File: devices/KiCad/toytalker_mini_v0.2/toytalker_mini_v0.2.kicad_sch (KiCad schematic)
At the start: 29 parts, among them J1 TYPE-C-31-M-12, J2 SM02B-SRSS-TB(LF)(SN), U1 BQ25185DLHR, U2 AP2112K-3.3TRG1, U3 ESP32-S3-MINI-1-N4R2, U4 MAX98357AEWL_T

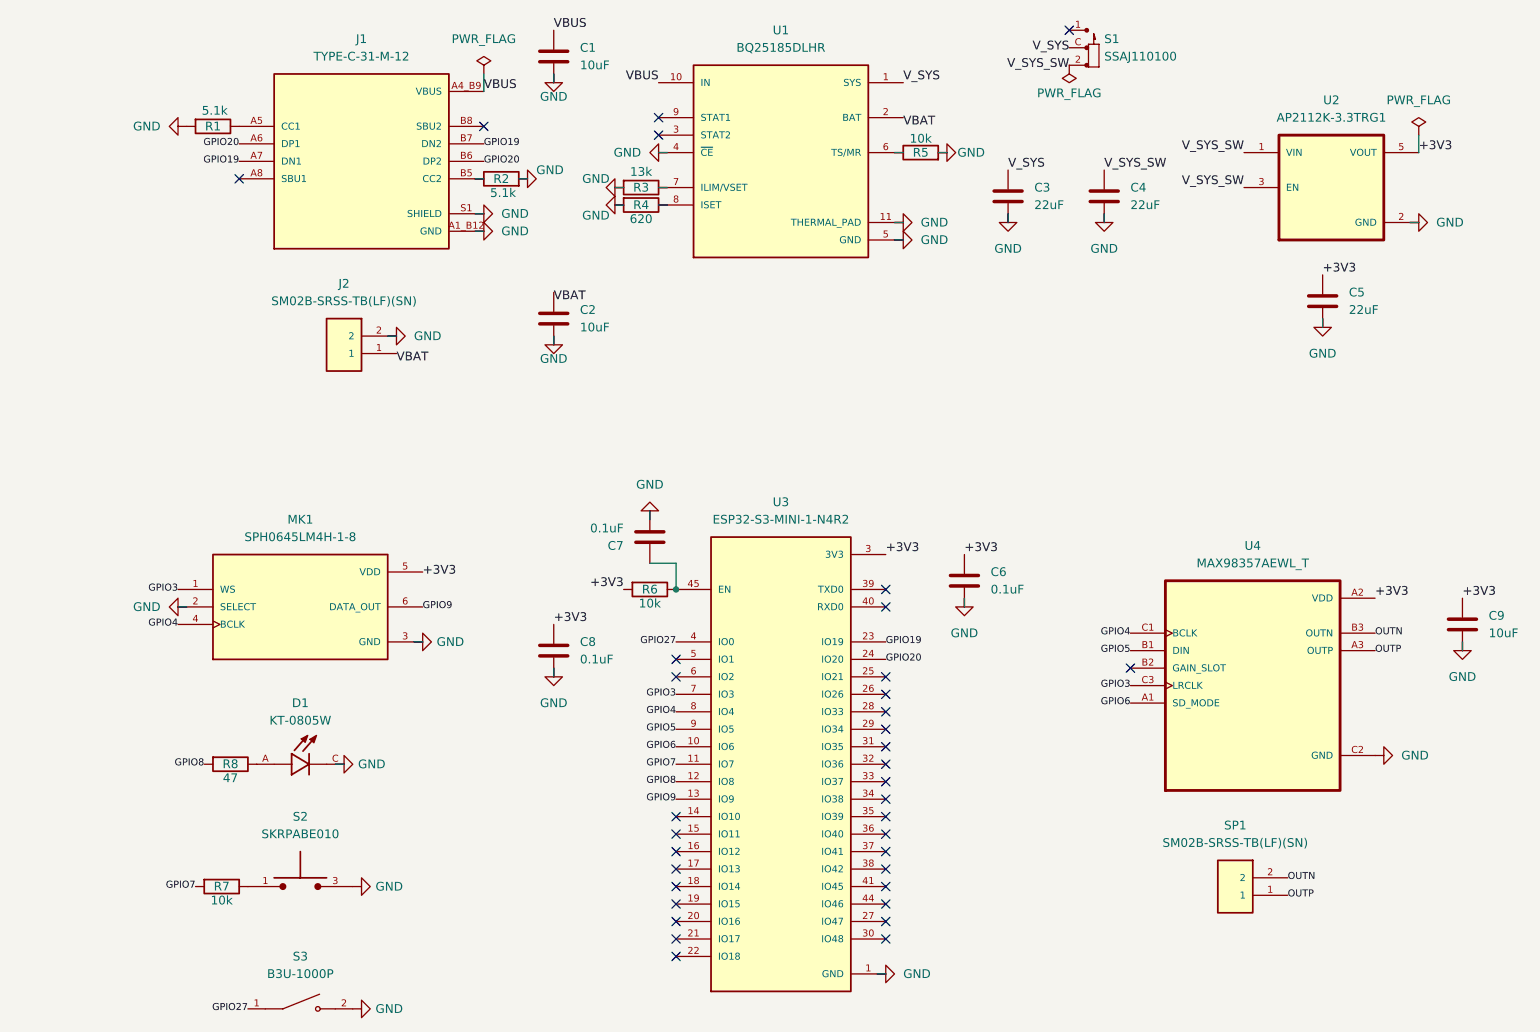
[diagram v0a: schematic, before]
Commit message: Complete v0.2 schematic: ERC clean, new parts, temp sensing, EN-mode power
- New connectors: J2=JST ZH (S2B-ZR-SM4A-TF), SP1=HC-1.25-2PWT (MX1.25),
  S1=MSK12C02G15-B slide switch in EN-mode (signal-only via PWR_EN + R9 100k)
- Charge temp protection: TH1 (NCP15XH103F03RC) on BQ25185 TS/MR
- Board temp readout: TH2 + R14 divider on GPIO2 (ADC1_CH1)
- Battery voltage divider on GPIO1, STAT1/2 to GPIO13/14 with 100k pullups
- LED R8 47R -> 470R, amp VDD direct to V_SYS, I2S pins separated
- Fix BQ25185 SYS pin type to power_out; footprint links now use
  project 'footprints' lib; register 3 missing symbol libs project-locally
- ERC: 0 errors, 0 warnings; all nets verified against PINMAP.md via netlist

Co-Authored-By: Claude Fable 5 <noreply@anthropic.com>
Claude-Session: https://claude.ai/code/session_017Se8MNjUgWCs8o61hRDxnG
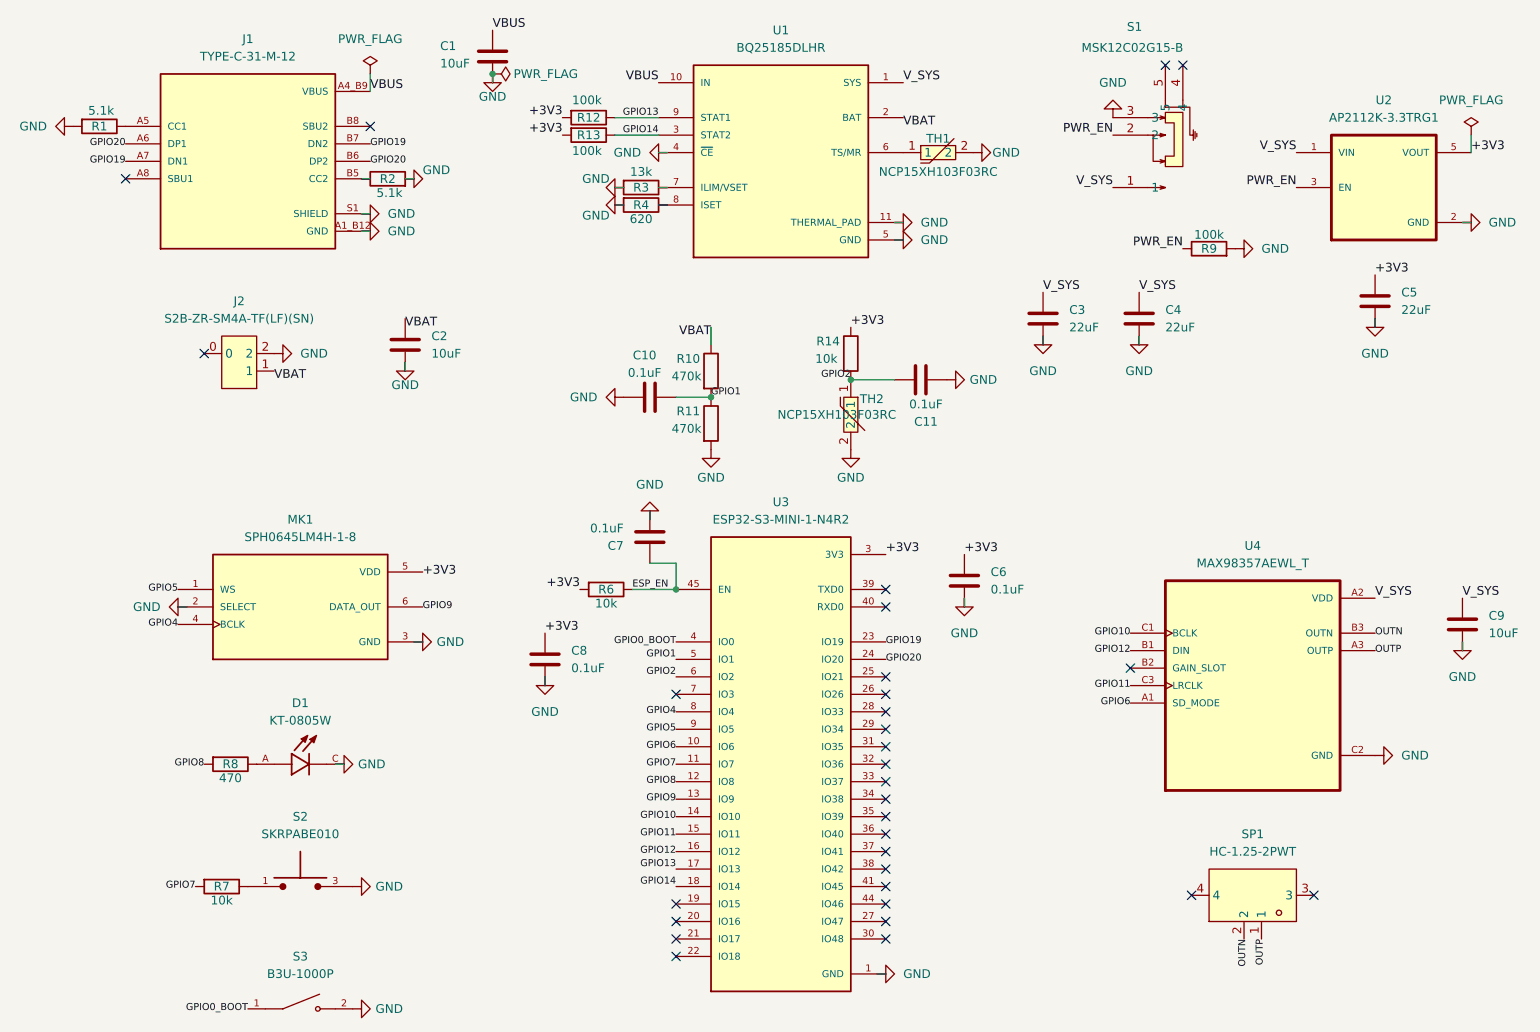
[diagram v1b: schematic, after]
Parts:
- removed J2, SP1: SM02B-SRSS-TB(LF)(SN), footprints:SM02B-SRSS-TB_LF__SN_, symbol SM02B-SRSS-TB_LF__SN_:SM02B-SRSS-TB_LF__SN_
- removed R5: 10k, Resistor_SMD:R_0402_1005Metric, symbol Device:R
- removed S1: SSAJ110100, footprints:SW_SSAJ110100, symbol SSAJ110100:SSAJ110100
- added C10, C11: 0.1uF, Capacitor_SMD:C_0603_1608Metric, symbol Device:C
- added J2: S2B-ZR-SM4A-TF(LF)(SN), toytalker_v02_parts:CONN-SMD_S2B-ZR-SM4A, symbol toytalker_v02_parts:S2B-ZR-SM4A-TF(LF)(SN)
- added R10, R11: 470k, Resistor_SMD:R_0402_1005Metric, symbol Device:R
- added R12, R13, R9: 100k, Resistor_SMD:R_0402_1005Metric, symbol Device:R
- added R14: 10k, Resistor_SMD:R_0402_1005Metric, symbol Device:R
- added S1: MSK12C02G15-B, toytalker_v02_parts:SW-SMD_MSK12C02G15-B, symbol toytalker_v02_parts:MSK12C02G15-B
- added SP1: HC-1.25-2PWT, toytalker_v02_parts:CONN-SMD_2P-P1.25-HC-1.25-2PWT, symbol toytalker_v02_parts:HC-1.25-2PWT
- added TH1, TH2: NCP15XH103F03RC, toytalker_v02_parts:R0402, symbol toytalker_v02_parts:NCP15XH103F03RC
- R8: value 47 -> 470
- S3: footprint Button_Switch_SMD:SW_SPST_B3U-1000P -> footprints:SW_B3U-1000P
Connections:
- net +3V3: now also R12.2, R13.2, R14.1; no longer C9.1, U4.A2 (VDD)
- net GND: now also C10.2, C11.2, J2.2, R11.2, R9.2, S1.3, TH1.2, TH2.2
- net GPIO4: no longer U4.C1 (BCLK)
- net GPIO5: now also MK1.1 (WS); no longer U4.B1 (DIN)
- net OUTN: now also SP1.2
- net OUTP: now also SP1.1
- net VBAT: now also J2.1, R10.1
- net V_SYS: now also C4.1, C9.1, U2.1 (VIN), U4.A2 (VDD), S1.1
- net at U1.6 (TS/MR): now also TH1.1
- net ESP_EN: now reaches C7.1, R6.1, U3.45 (EN)
- net GPIO10: now reaches U3.14 (IO10)
- net GPIO10: now also U4.C1 (BCLK)
- net GPIO11: now reaches U3.15 (IO11)
- net GPIO11: now also U4.C3 (LRCLK)
- net GPIO12: now reaches U3.16 (IO12)
- net GPIO12: now also U4.B1 (DIN)
- net GPIO13: now reaches U3.17 (IO13)
- net GPIO13: now also U1.9 (STAT1), R12.1
- net GPIO14: now reaches U3.18 (IO14)
- net GPIO14: now also U1.3 (STAT2), R13.1
- net GPIO1: now reaches U3.5 (IO1)
- net GPIO1: now also C10.1, R10.2, R11.1
- net GPIO2: now reaches U3.6 (IO2)
- net GPIO2: now also C11.1, R14.2, TH2.1
- net GPIO27 renamed GPIO0_BOOT
- removed net GPIO3: MK1.1 (WS), U3.7 (IO3), U4.C3 (LRCLK)
- removed net V_SYS_SW: C4.1, U2.1 (VIN), U2.3 (EN)
- new net PWR_EN: R9.1, S1.2, U2.3 (EN)
- no-connect marks 35 -> 31
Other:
- moved on the sheet: C1, C2, C3, C4, C5, C8, J1, R1, R2, R6, U2

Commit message: Reassign 9 signal pins for routing-optimal layout; add full route plan
- Pins chosen from final hand placement: mic I2S -> IO33/34/48 (left column
  bottom, 4mm west to mic), amp I2S+SD -> IO36-39 (bottom row, south lane),
  BUTTON -> IO35, LED -> IO47; ADC/BOOT/USB/STAT/EN unchanged
- Schematic labels moved via computed pin endpoints; ERC 0/0; netlist diff
  verified: exactly 9 nets changed, old GPIO4-12 nets eliminated
- PINMAP.md: new table + firmware defines (v0.5)
- LAYOUT_PLAN.md: per-net route table (22 nets) with corridor width math
  and B-side jump ledger (7 entries, all west of module, none under RF)
- PARTS_LIST.md: package size rationale (0402/0603 usage rules)

Co-Authored-By: Claude Fable 5 <noreply@anthropic.com>
Claude-Session: https://claude.ai/code/session_017Se8MNjUgWCs8o61hRDxnG
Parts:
- C10, C11: footprint Capacitor_SMD:C_0603_1608Metric -> Capacitor_SMD:C_0402_1005Metric
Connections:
- net GPIO47: now reaches U3.27 (IO47)
- net GPIO47: now also R8.2
- net GPIO33: now reaches U3.28 (IO33)
- net GPIO33: now also MK1.1 (WS)
- net GPIO34: now reaches U3.29 (IO34)
- net GPIO34: now also MK1.6 (DATA_OUT)
- net GPIO48: now reaches U3.30 (IO48)
- net GPIO48: now also MK1.4 (BCLK)
- net GPIO35: now reaches U3.31 (IO35)
- net GPIO35: now also R7.2
- net GPIO36: now reaches U3.32 (IO36)
- net GPIO36: now also U4.C1 (BCLK)
- net GPIO37: now reaches U3.33 (IO37)
- net GPIO37: now also U4.C3 (LRCLK)
- net GPIO38: now reaches U3.34 (IO38)
- net GPIO38: now also U4.B1 (DIN)
- net GPIO39: now reaches U3.35 (IO39)
- net GPIO39: now also U4.A1 (SD_MODE)
- net GPIO10: no longer names the net of U3.14 (IO10)
- net GPIO10: no longer U4.C1 (BCLK)
- net GPIO11: no longer names the net of U3.15 (IO11)
- net GPIO11: no longer U4.C3 (LRCLK)
- net GPIO12: no longer names the net of U3.16 (IO12)
- net GPIO12: no longer U4.B1 (DIN)
- net GPIO4: no longer names the net of U3.8 (IO4)
- net GPIO4: no longer MK1.4 (BCLK)
- net GPIO5: no longer names the net of U3.9 (IO5)
- net GPIO5: no longer MK1.1 (WS)
- net GPIO6: no longer names the net of U3.10 (IO6)
- net GPIO6: no longer U4.A1 (SD_MODE)
- net GPIO7: no longer names the net of U3.11 (IO7)
- net GPIO7: no longer R7.2
- net GPIO8: no longer names the net of U3.12 (IO8)
- net GPIO8: no longer R8.2
- net GPIO9: no longer names the net of U3.13 (IO9)
- net GPIO9: no longer MK1.6 (DATA_OUT)
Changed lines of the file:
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@@
 	)
 	(no_connect
-		(at 153.67 147.32)
-	)
-	(no_connect
 		(at 123.19 142.24)
 	)
@@
 	)
 	(no_connect
-		(at 153.67 127)
-	)
-	(no_connect
 		(at 196.85 20.32)
 	)
@@
 	)
 	(no_connect
-		(at 153.67 124.46)
-	)
-	(no_connect
 		(at 198.12 140.97)
 	)
@@
 	)
 	(no_connect
-		(at 153.67 119.38)
-	)
-	(no_connect
-		(at 153.67 114.3)
-	)
-	(no_connect
-		(at 153.67 121.92)
-	)
-	(no_connect
 		(at 78.74 29.21)
 	)
 	(no_connect
-		(at 153.67 129.54)
-	)
-	(no_connect
 		(at 43.18 36.83)
 	)
@@
 	)
 	(no_connect
-		(at 153.67 144.78)
-	)
-	(no_connect
 		(at 123.19 149.86)
 	)
@@
 	)
 	(no_connect
-		(at 153.67 116.84)
-	)
-	(no_connect
 		(at 153.67 109.22)
 	)
@@
 		)
 	)
-	(label "GPIO6"
+	(label "GPIO39"
 		(at 189.23 113.03 180)
 		(effects
@@
 		)
 	)
-	(label "GPIO6"
-		(at 123.19 119.38 180)
-		(effects
-			(font
-				(size 1.016 1.016)
-			)
-			(justify right)
-		)
-	)
 	(label "+3V3"
 		(at 109.22 96.52 180)
@@
 		)
 	)
-	(label "GPIO10"
+	(label "GPIO36"
 		(at 189.23 102.87 180)
 		(effects
@@
 		)
 	)
-	(label "GPIO8"
-		(at 123.19 124.46 180)
-		(effects
-			(font
-				(size 1.016 1.016)
-			)
-			(justify right)
-		)
-	)
 	(label "V_SYS"
 		(at 190.5 53.34 0)
@@
 		)
 	)
-	(label "GPIO11"
-		(at 123.19 132.08 180)
-		(effects
-			(font
-				(size 1.016 1.016)
-			)
-			(justify right)
-		)
-	)
 	(label "GPIO20"
 		(at 43.18 31.75 180)
@@
 		)
 	)
-	(label "GPIO12"
+	(label "GPIO38"
 		(at 189.23 105.41 180)
 		(effects
@@
 		)
 	)
-	(label "GPIO7"
+	(label "GPIO35"
 		(at 53.34 139.7 180)
 		(effects
@@
 		)
 	)
-	(label "GPIO4"
-		(at 123.19 114.3 180)
-		(effects
-			(font
-				(size 1.016 1.016)
-			)
-			(justify right)
-		)
-	)
 	(label "OUTP"
 		(at 208.28 147.32 270)
@@
 		)
 	)
-	(label "GPIO8"
+	(label "GPIO47"
 		(at 54.61 121.92 180)
 		(effects
@@
 		)
 	)
-	(label "GPIO4"
+	(label "GPIO48"
 		(at 50.8 101.6 180)
 		(effects
@@
 		)
 	)
-	(label "GPIO10"
-		(at 123.19 129.54 180)
-		(effects
-			(font
-				(size 1.016 1.016)
-			)
-			(justify right)
-		)
-	)
 	(label "PWR_EN"
 		(at 213.36 38.1 180)
@@
 		)
 	)
-	(label "GPIO9"
+	(label "GPIO34"
 		(at 86.36 99.06 0)
 		(effects
@@
 		)
 	)
-	(label "GPIO9"
-		(at 123.19 127 180)
-		(effects
-			(font
-				(size 1.016 1.016)
-			)
-			(justify right)
-		)
-	)
 	(label "VBAT"
 		(at 83.82 57.15 0)
@@
 		)
 	)
-	(label "GPIO11"
+	(label "GPIO37"
 		(at 189.23 110.49 180)
 		(effects
@@
 		)
 	)
-	(label "GPIO5"
+	(label "GPIO33"
 		(at 50.8 96.52 180)
 		(effects
@@
 		)
 	)
-	(label "GPIO7"
-		(at 123.19 121.92 180)
-		(effects
-			(font
-				(size 1.016 1.016)
-			)
-			(justify right)
-		)
-	)
-	(label "GPIO5"
-		(at 123.19 116.84 180)
-		(effects
-			(font
-				(size 1.016 1.016)
-			)
-			(justify right)
-		)
-	)
 	(label "+3V3"
 		(at 224.79 50.8 0)
@@
 		)
 	)
-	(label "GPIO12"
-		(at 123.19 134.62 180)
-		(effects
-			(font
-				(size 1.016 1.016)
-			)
-			(justify right)
-		)
-	)
 	(symbol
 		(lib_id "power:PWR_FLAG")
@@
 			)
 		)
-		(property "Footprint" "Capacitor_SMD:C_0603_1608Metric"
+		(property "Footprint" "Capacitor_SMD:C_0402_1005Metric"
 			(at 162.56 65.0748 0)
 			(hide yes)
@@
 			)
 		)
-		(property "Footprint" "Capacitor_SMD:C_0603_1608Metric"
+		(property "Footprint" "Capacitor_SMD:C_0402_1005Metric"
 			(at 115.57 69.5452 0)
 			(hide yes)
@@
 	)
 	(embedded_fonts no)
+	(no_connect
+		(at 123.19 114.3)
+	)
+	(label "GPIO48"
+		(at 153.67 147.32 0)
+		(effects
+			(font
+				(size 1.27 1.27)
+			)
+			(justify left bottom)
+		)
+	)
+	(no_connect
+		(at 123.19 116.84)
+	)
+	(label "GPIO33"
+		(at 153.67 114.3 0)
+		(effects
+			(font
+				(size 1.27 1.27)
+			)
+			(justify left bottom)
+		)
+	)
+	(no_connect
+		(at 123.19 127.0)
+	)
+	(label "GPIO34"
+		(at 153.67 116.84 0)
+		(effects
+			(font
+				(size 1.27 1.27)
+			)
+			(justify left bottom)
+		)
+	)
+	(no_connect
+		(at 123.19 119.38)
+	)
+	(label "GPIO39"
+		(at 153.67 129.54 0)
+		(effects
+			(font
+				(size 1.27 1.27)
+			)
+			(justify left bottom)
+		)
+	)
+	(no_connect
+		(at 123.19 121.92)
+	)
+	(label "GPIO35"
+		(at 153.67 119.38 0)
+		(effects
+			(font
+				(size 1.27 1.27)
+			)
+			(justify left bottom)
+		)
+	)
+	(no_connect
+		(at 123.19 124.46)
+	)
+	(label "GPIO47"
+		(at 153.67 144.78 0)
+		(effects
+			(font
+				(size 1.27 1.27)
+			)
+			(justify left bottom)
+		)
+	)
+	(no_connect
+		(at 123.19 129.54)
+	)
+	(label "GPIO36"
+		(at 153.67 121.92 0)
+		(effects
+			(font
+				(size 1.27 1.27)
+			)
+			(justify left bottom)
+		)
+	)
+	(no_connect
+		(at 123.19 132.08)
+	)
+	(label "GPIO37"
+		(at 153.67 124.46 0)
+		(effects
+			(font
+				(size 1.27 1.27)
+			)
+			(justify left bottom)
+		)
+	)
+	(no_connect
+		(at 123.19 134.62)
+	)
+	(label "GPIO38"
+		(at 153.67 127.0 0)
+		(effects
+			(font
+				(size 1.27 1.27)
+			)
+			(justify left bottom)
+		)
+	)
 )

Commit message: Move LED to IO40; placement QA complete, all decap distances pass
- LED reassigned IO47->IO40 (bottom row): IO47's west path to R8 was
  blocked by C9/S2/MK1 gaps (3 routes checked); IO40 rides the S2-east
  lane with the amp bundle, no B-side jump needed
- ERC 0/0, netlist verified: /GPIO40={R8-2,U3-36}, GPIO47 eliminated
- User rework: C1 to 2.2mm from U1.IN with VBUS reroute, C2 4.1mm,
  CC resistors tucked to J1, TH1 relocated away from charger heat
  (19mm, fixes self-heating false charge-stop), TH2 near module kept
  as deliberate ESP32-area sensor (paired with internal die sensor)
- Fixed C10/C11 footprint symbol-link corruption from earlier template
  copy (duplicate C6/C11 removed, links repaired)

Co-Authored-By: Claude Fable 5 <noreply@anthropic.com>
Claude-Session: https://claude.ai/code/session_017Se8MNjUgWCs8o61hRDxnG
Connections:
- net GPIO40: now reaches U3.36 (IO40)
- net GPIO40: now also R8.2
- net GPIO47: no longer names the net of U3.27 (IO47)
- net GPIO47: no longer R8.2
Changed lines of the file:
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@@
 	)
 	(no_connect
-		(at 153.67 132.08)
-	)
-	(no_connect
 		(at 153.67 109.22)
 	)
@@
 		)
 	)
-	(label "GPIO47"
+	(label "GPIO40"
 		(at 54.61 121.92 180)
 		(effects
@@
 		(effects
 			(font
-				(size 1.27 1.27)
+				(size 1.016 1.016)
 			)
 			(justify left bottom)
@@
 		(effects
 			(font
-				(size 1.27 1.27)
+				(size 1.016 1.016)
 			)
 			(justify left bottom)
@@
 		(effects
 			(font
-				(size 1.27 1.27)
+				(size 1.016 1.016)
 			)
 			(justify left bottom)
@@
 		(effects
 			(font
-				(size 1.27 1.27)
+				(size 1.016 1.016)
 			)
 			(justify left bottom)
@@
 		(effects
 			(font
-				(size 1.27 1.27)
+				(size 1.016 1.016)
 			)
 			(justify left bottom)
@@
 		(at 123.19 124.46)
 	)
-	(label "GPIO47"
-		(at 153.67 144.78 0)
-		(effects
-			(font
-				(size 1.27 1.27)
-			)
-			(justify left bottom)
-		)
-	)
 	(no_connect
 		(at 123.19 129.54)
@@
 		(effects
 			(font
-				(size 1.27 1.27)
+				(size 1.016 1.016)
 			)
 			(justify left bottom)
@@
 		(effects
 			(font
-				(size 1.27 1.27)
+				(size 1.016 1.016)
 			)
 			(justify left bottom)
@@
 		(effects
 			(font
-				(size 1.27 1.27)
+				(size 1.016 1.016)
+			)
+			(justify left bottom)
+		)
+	)
+	(no_connect
+		(at 153.67 144.78)
+	)
+	(label "GPIO40"
+		(at 153.67 132.08 0)
+		(effects
+			(font
+				(size 1.016 1.016)
 			)
 			(justify left bottom)

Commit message: Complete v0.2 routing: all nets routed, GND fully stitched, DRC clean
- All 66 nets routed (user hand-routing + planned B-side jumps, all
  west of module; ESP32 underside and antenna B.Cu kept pristine)
- GND infrastructure: 9-via thermal farm under ESP32 (datasheet land
  pattern), 4 antenna-side stitch vias (Espressif HW guideline), solid
  zone connects on U3/U1/MK1/J1, U1 thermal holes net-assigned,
  TH1/TH2 thermal vias, 20+ stitch vias for isolated pour pockets
- Fixed 4 isolated GND clusters found by union-find connectivity
  analysis (incl. U1 charger group fenced in by B-side jumps; final
  link found by BFS maze-solver on B.Cu)
- Legacy v0.1 antenna keepouts stranded off-board inside U3 footprint
  removed; via standards normalized via netclasses (0.5/0.3, pwr 0.6/0.3)
- Remaining DRC items are known-benign only (connector-at-edge, WLP
  mask slivers, switch peg annulars, silk cosmetics)

Co-Authored-By: Claude Fable 5 <noreply@anthropic.com>
Claude-Session: https://claude.ai/code/session_017Se8MNjUgWCs8o61hRDxnG
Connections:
- net GPIO36: now also U4.C3 (LRCLK); no longer U4.C1 (BCLK)
- net GPIO37: now also U4.C1 (BCLK); no longer U4.C3 (LRCLK)
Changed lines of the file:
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@@
 		)
 	)
-	(label "GPIO36"
+	(label "GPIO37"
 		(at 189.23 102.87 180)
 		(effects
@@
 		)
 	)
-	(label "GPIO37"
+	(label "GPIO36"
 		(at 189.23 110.49 180)
 		(effects
